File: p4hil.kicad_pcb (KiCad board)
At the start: 4 copper layers, 81.3 x 61 mm, 227 parts, among them J1 Conn_02x02_Odd_Even, J10 Conn_01x20, J11 Conn_01x20, J12 Conn_01x20, J13 USB_A_Stacked, J14 Conn_01x04, J15 Conn_01x20, J16 Conn_01x04, J17 Barrel_Jack_Switch, J18 Conn_02x05_Odd_Even, J19 HR871150C, J2 Conn_01x08, J20 Conn_02x04_Odd_Even, J21 Conn_01x06, J3 USB_C_Receptacle_USB2.0_16P, J4 Conn_01x10, J5 Conn_01x20, J6 Conn_01x20, J7 Conn_01x20, J8 Conn_01x02, J9 Conn_01x06, SW1 SW_Push, SW2 SW_Push, U1 W25Q128JVS, U10 TLV62569DBV, U11 MT9700_SY6280, U3 TLV62569DBV, U4 IPGRI, U5 PI4IOE5V9535ZDEX, U6 INA219AxD, U7 CH334F, U8 MT9700_SY6280, U9 MT9700_SY6280, Y1 40MHz(+-10 ppm) C501798, Y2 25Mhz 12pf, Y3 12MHz

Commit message: silkscreen
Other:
- board text added: "10"
- board text added: "11"
- board text added: "12"
- board text added: "13"
- board text added: "14"
- board text added: "15"
- board text added: "16"
- board text added: "17"
- board text added: "18"
- board text added: "19"
- board text added: "20"
- board text added: "5"
- board text added: "6"
- board text added: "7"
- board text added: "8"
- board text added: "9"
- board text added: "<Start Here"
- board text added: "Arduino Uno"
- board text added: "B"
- board text added: "DC Jack"
- board text added: "External Regulator For >5V In"
- board text added: "Feather"
- board text added: "GND"
- board text added: "Nano"
- board text added: "Pico"
- board text added: "Pro Micro"
- board text added: "QTPy XIAO"
- board text added: "T"
- board text added: "Trinket"
- board text added: "V"
- board text added: "x G 3+ 3- V G G 4+ 4- V"

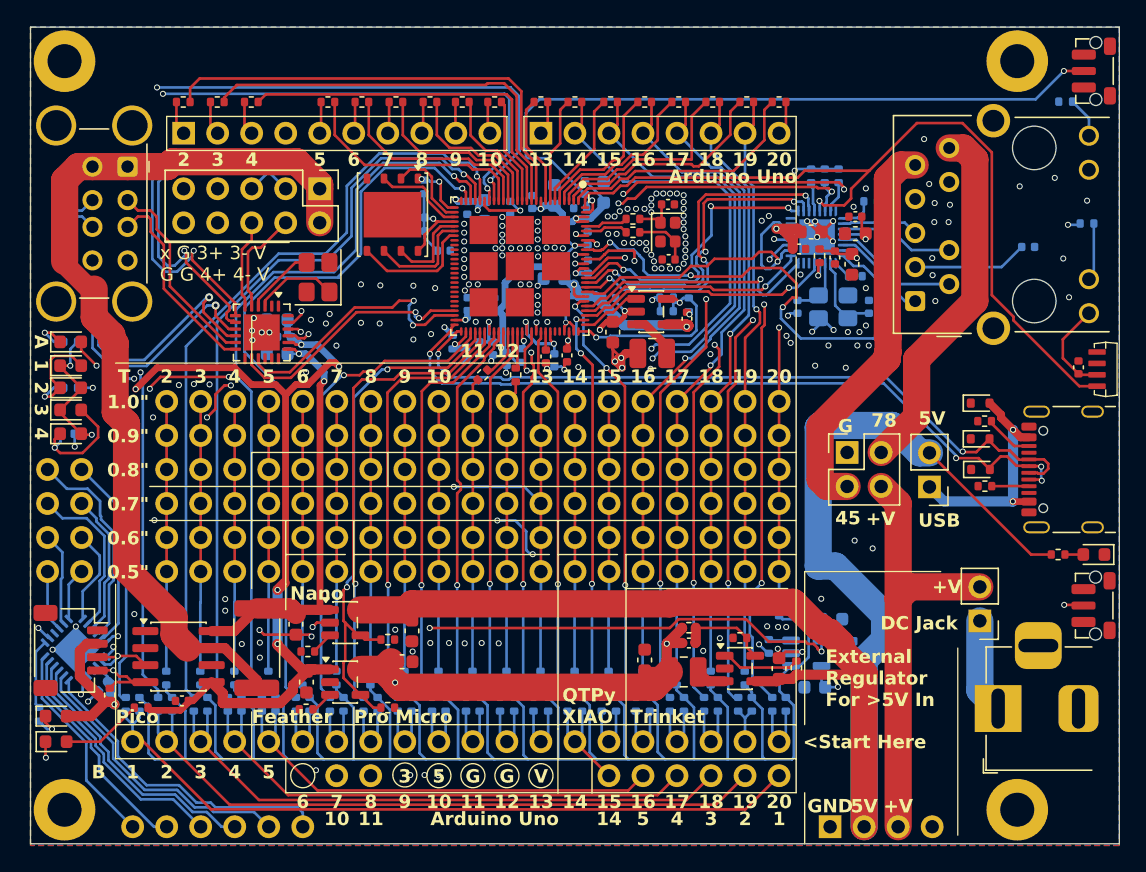
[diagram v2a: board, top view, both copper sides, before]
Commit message: Connect flash VDD and more silkscreen
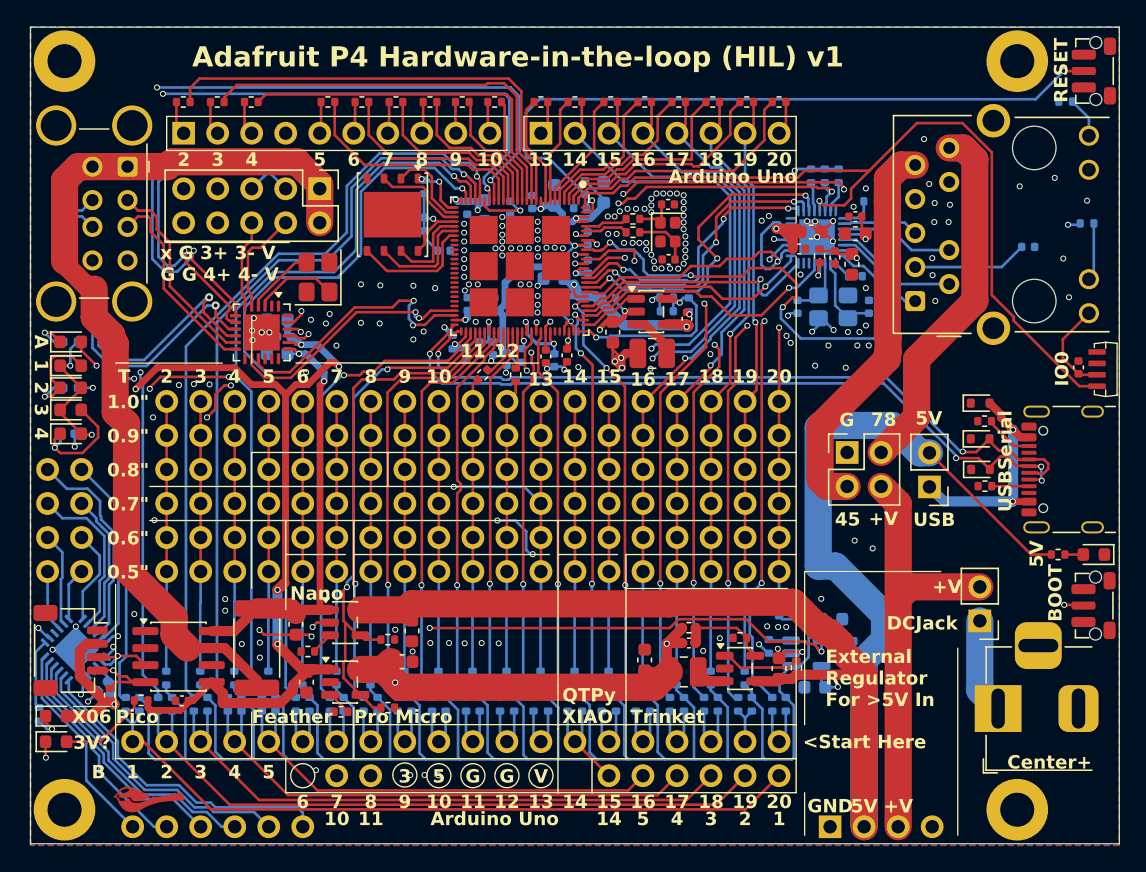
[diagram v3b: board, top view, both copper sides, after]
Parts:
- added G***: LOGO, chickadee:chickadee_2mm_fcu, F.Cu at (112.9, 124.7)
- moved R21 2.61 mm to (127.3, 118.1)
- moved R93 0.54 mm to (112.4, 117.3)
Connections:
- C25 pad 1: /P4/VDDO_FLASH -> /P4/VDD_FLASH
- U2 pad 71: /P4/VDDO_FLASH -> /P4/VDD_FLASH
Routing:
- net /P4/VDD_FLASH: track 9.81 -> 31.4 mm, vias 1 -> 2
- net /B13: track 29.5 -> 32.6 mm
- net /Ethernet/RMII_RXD0: track 24.6 -> 22.6 mm
- net /Ethernet/RMII_RXD1: track 22.5 -> 20.9 mm
- net /P4/VDDO_FLASH: track 1.39 -> 0.00 mm
- net /Ethernet/RMII_TXEN: track 19.2 -> 20.5 mm
- net +3.3V: track 258.3 -> 259.1 mm
- net /B15: track 29.8 -> 30.6 mm
- net /B19: track 44.5 -> 43.9 mm
- net /Ethernet/RMII_TXD0: track 17.5 -> 18.0 mm
- net /USB Host/SWITCHED_3V3: track 70.2 -> 70.7 mm
- net Net-(D9-A): track 6.10 -> 6.64 mm
- net /Ethernet/RMII_CRSDV: track 25.9 -> 25.4 mm
- net GND: vias 181 -> 180
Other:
- board text added: "3V?"
- board text added: "Adafruit P4 Hardware-in-the-loop (HIL) v1"
- board text added: "BOOT"
- board text added: "Center+"
- board text added: "DCJack"
- board text added: "IO0"
- board text added: "RESET"
- board text added: "USBSerial"
- board text added: "~{X06}"
- board text removed: "DC Jack"

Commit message: v1
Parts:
- R16, R17: value 220 -> 4.7K
- R18: value 470 -> 47K
- R26, R93: value 2.2K -> 4.7K
- R73: value 470 -> 4.7K
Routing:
- net /Ethernet/RMII_TXD0: track 18.0 -> 23.4 mm
- net /Ethernet/RMII_TXD1: track 19.0 -> 23.4 mm
- net /Ethernet/RMII_TXEN: track 20.5 -> 23.3 mm
- net /P4/FB_DCDC: track 15.7 -> 17.2 mm
- net /Ethernet/RMII_CRSDV: track 25.4 -> 24.2 mm
- net /DeviceUnderTest/T19i: track 40.3 -> 39.5 mm
- net /PHY_RESETN: track 37.6 -> 38.3 mm
